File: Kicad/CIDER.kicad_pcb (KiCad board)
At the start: 4 copper layers, 74.9 x 57.1 mm, 69 parts, among them CN1 CDTV-DIAG, J1 JTAG, J2 LED, J3 A500_MODE, J4 Conn_02x22_Odd_Even, J5 To JP15, SW1 SW_DIP_x04, U1 AZ1117-3.3, U10 SST39SF010, U11 74LVC1G32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

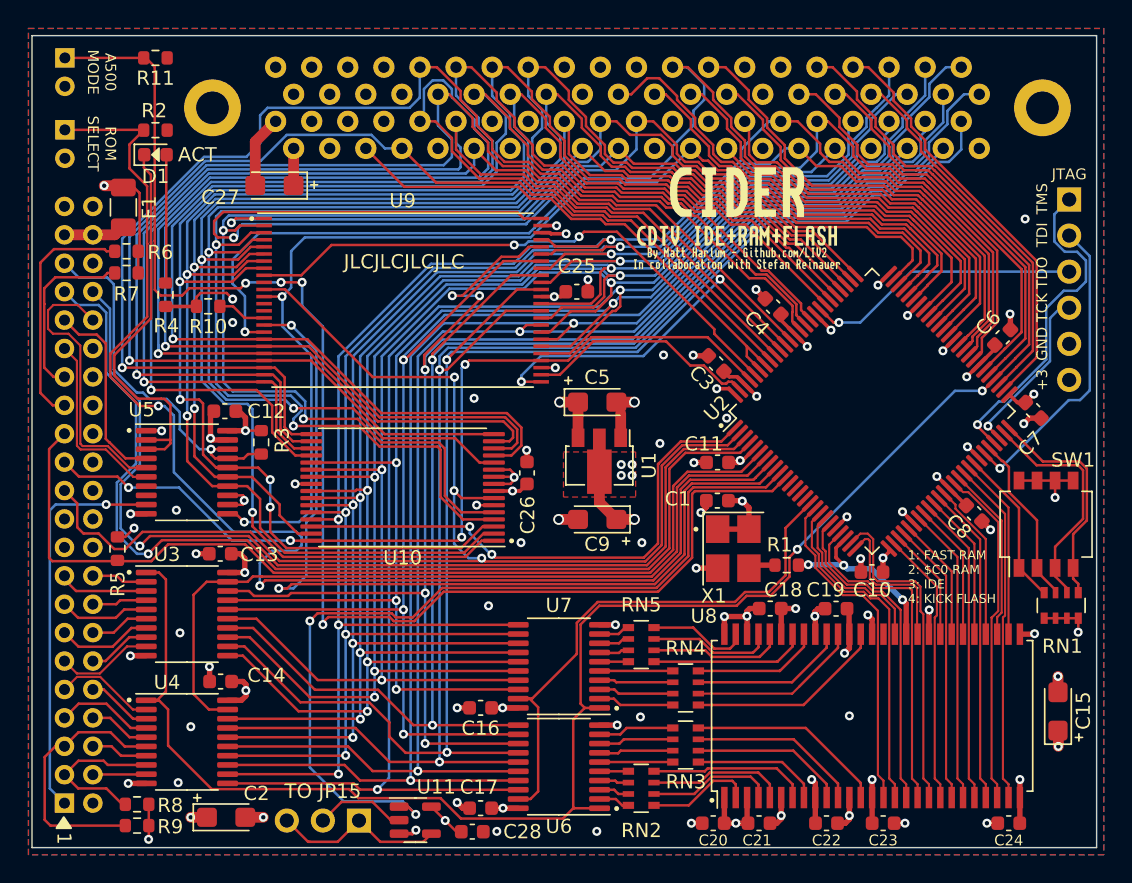
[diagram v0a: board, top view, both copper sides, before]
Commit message: Rev_A1: Add pull-down resistor for U11 input, add tooling holes
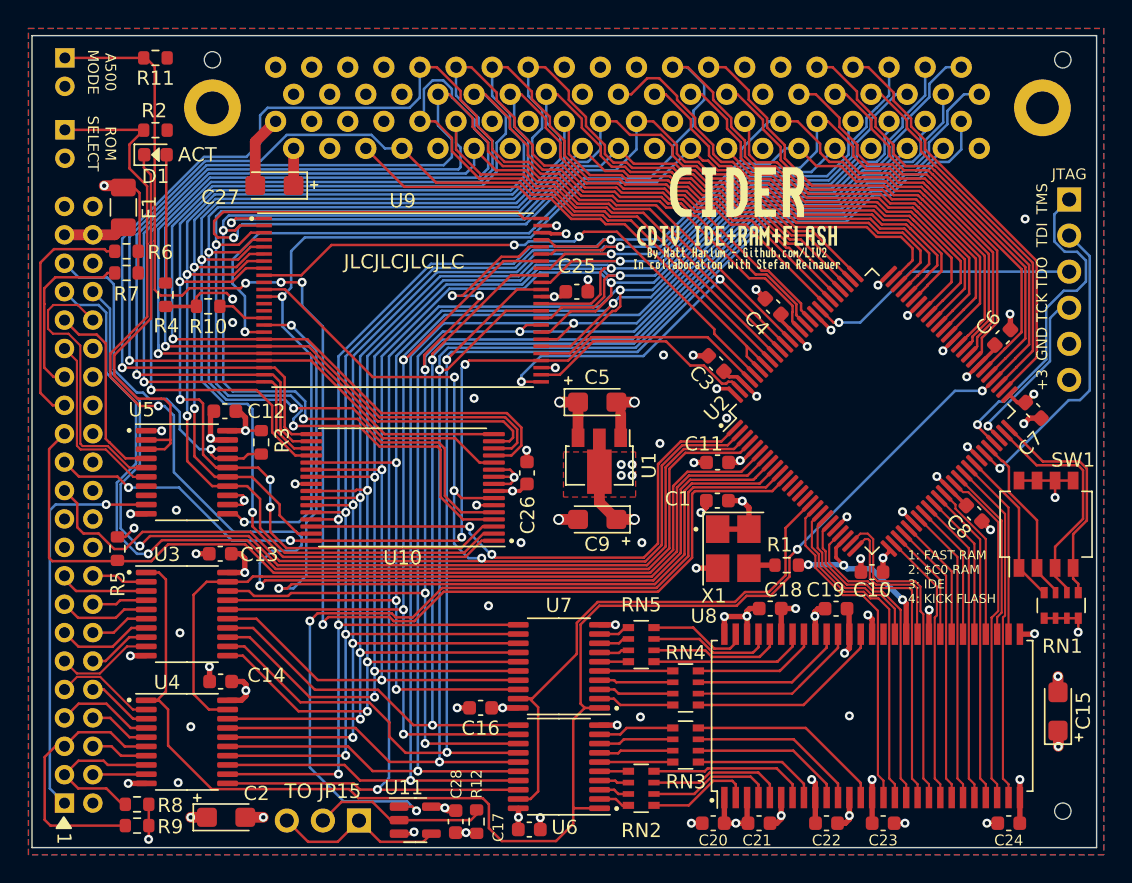
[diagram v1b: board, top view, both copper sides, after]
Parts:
- added ?: , , F.Cu at (178.0, 95.7)
- added R12: 10K, Resistor_SMD:R_0603_1608Metric, F.Cu at (136.7, 149.3)
- added REF**: jlc_assembly_toolinghole, JLC-Tooling:jlc_assembly_toolinghole, F.Cu at (178.0, 148.6)
- added REF**: jlc_assembly_toolinghole, JLC-Tooling:jlc_assembly_toolinghole, F.Cu at (118.1, 95.7)
- moved C17 3.74 mm to (140.4, 149.9), turned to 0 degrees
- moved C28 1.37 mm to (135.2, 149.3), turned to -90 degrees
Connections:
- net /Amiga+CPLD/NOEXT renamed /Amiga+CPLD/A500
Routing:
- net Net-(J5-Pad2): track 6.44 -> 12.4 mm
- net /Amiga+CPLD/R~{W}: track 130.7 -> 133.6 mm
- net VCC: track 43.8 -> 41.9 mm
- net GND: track 85.2 -> 86.2 mm, vias 70 -> 69
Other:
- board text added: "REV A1 APR 2023"
- board text removed: "REV A APR 2023"

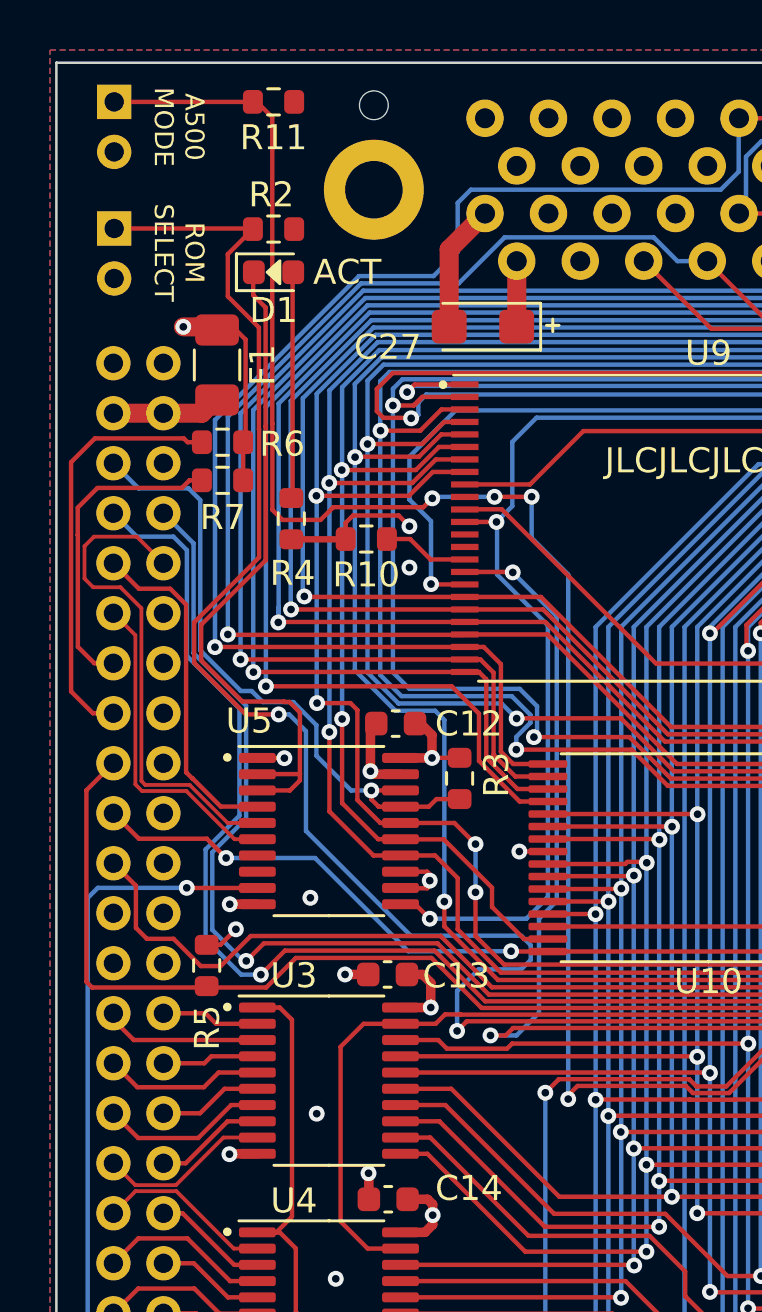
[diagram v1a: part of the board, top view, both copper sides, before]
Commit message: Rev-A1: Buffer A500/Bank Sel switches
Added inline resistors to these two and buffer them via U5
In Proto A it was found that operating the switches would cause latch-up and destroy the CPLD
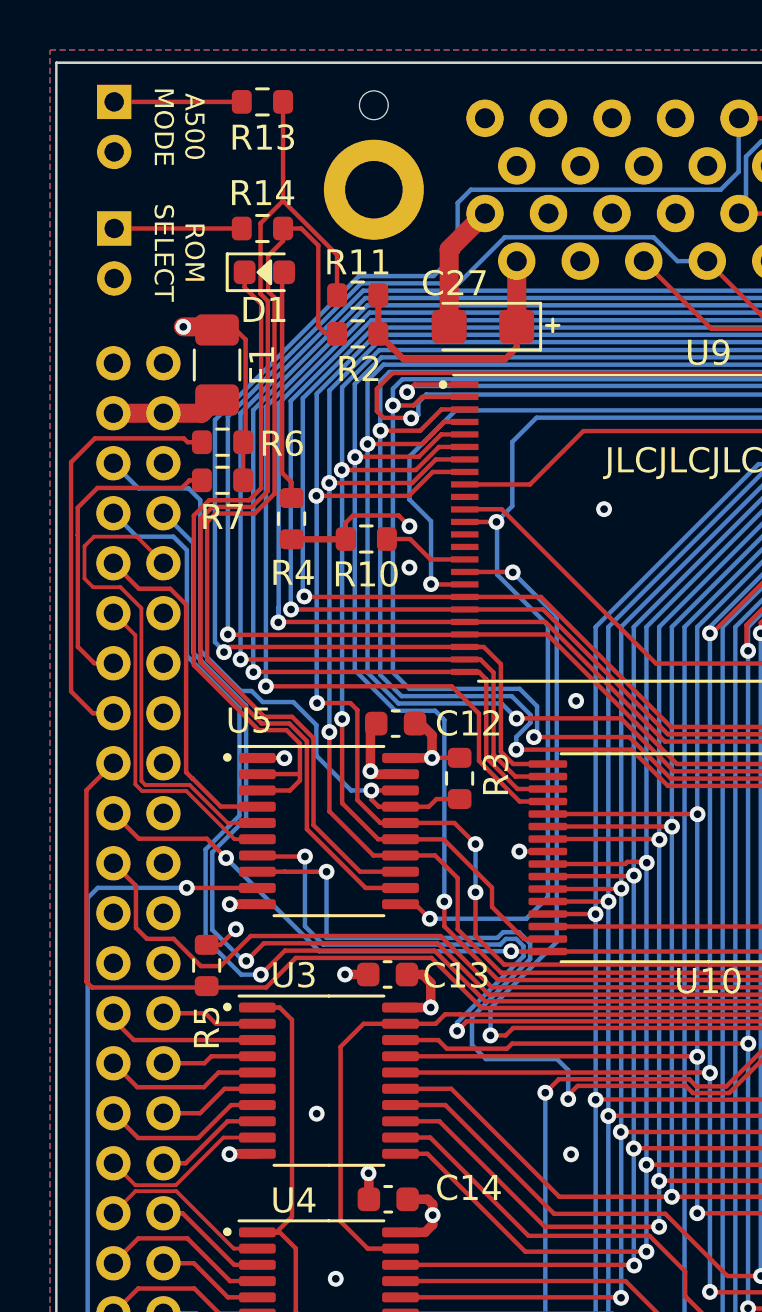
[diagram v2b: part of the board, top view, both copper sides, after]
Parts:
- added R13: 1K, Resistor_SMD:R_0603_1608Metric, F.Cu at (113.7, 95.5)
- added R14: 1K, Resistor_SMD:R_0603_1608Metric, F.Cu at (113.7, 100.6)
- U1: value AZ1117-3.3 -> AZ1117CR-3.3
- moved R11 8.43 mm to (117.5, 103.3)
- moved R2 5.38 mm to (117.5, 104.8)
- moved D1 0.37 mm to (113.7, 102.4)
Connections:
- J2 pad 1: /Amiga+CPLD/FLASH_BANK -> Net-(J2-Pad1)
- J2 pad 2: VCC -> GND
- J3 pad 1: /Amiga+CPLD/A500 -> Net-(J3-Pad1)
- J3 pad 2: VCC -> GND
- R11 pad 1: GND -> VCC
- R11 pad 2: /Amiga+CPLD/A500 -> /Amiga+CPLD/A500_SW
- R2 pad 1: GND -> VCC
- R2 pad 2: /Amiga+CPLD/FLASH_BANK -> /Amiga+CPLD/FLASH_BANK_SW
- U5 pad 12: GND -> /Amiga+CPLD/A500_SW
- U5 pad 13: GND -> /Amiga+CPLD/FLASH_BANK_SW
- U5 pad 7: unconnected-(U5-Pad7) -> /Amiga+CPLD/FLASH_BANK
- U5 pad 8: unconnected-(U5-Pad8) -> /Amiga+CPLD/A500
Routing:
- net /Amiga+CPLD/A500_SW: track 0.00 -> 43.4 mm
- net /Amiga+CPLD/FLASH_BANK_SW: track 0.00 -> 38.7 mm
- net /Amiga+CPLD/A500: track 97.5 -> 64.2 mm, vias 4 -> 2
- net /Amiga+CPLD/FLASH_BANK: track 93.1 -> 60.5 mm
- net VCC: track 41.9 -> 50.4 mm
- net Net-(J3-Pad1): track 0.00 -> 5.10 mm
- net Net-(J2-Pad1): track 0.00 -> 5.10 mm
- net GND: track 86.2 -> 83.3 mm, vias 69 -> 70
- net /IDE/~{LED}: track 27.9 -> 28.6 mm
- net /Amiga+CPLD/FLASH_A18: track 64.0 -> 63.3 mm

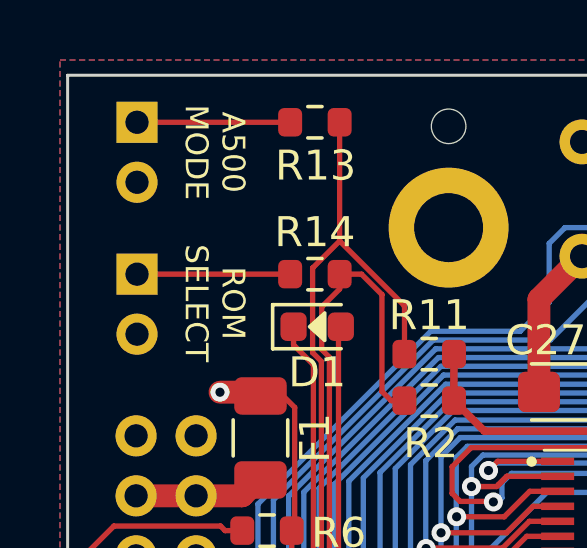
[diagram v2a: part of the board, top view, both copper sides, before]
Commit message: Rev-A1: move switch headers to top of the board and update render
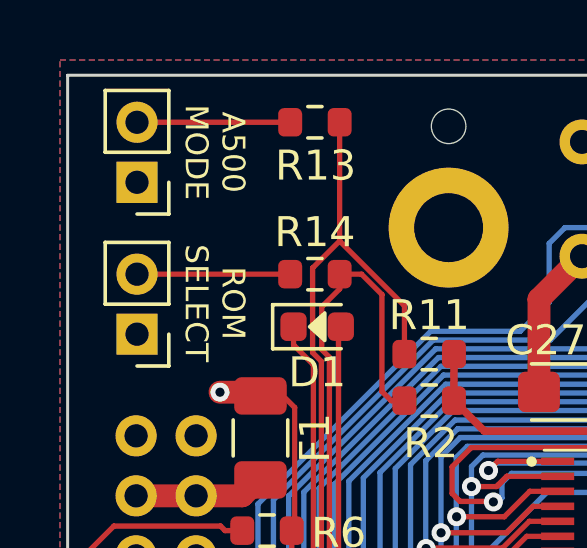
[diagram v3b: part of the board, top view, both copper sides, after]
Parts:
- J2, J3: moved to F.Cu
- moved J2 2.00 mm to (107.7, 102.6)
- moved J3 2.00 mm to (107.7, 97.5)
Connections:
- J2 pad 1: Net-(J2-Pad1) -> GND
- J2 pad 2: GND -> Net-(J2-Pad2)
- J3 pad 1: Net-(J3-Pad1) -> GND
- J3 pad 2: GND -> Net-(J3-Pad2)
- R13 pad 2: Net-(J3-Pad1) -> Net-(J3-Pad2)
- R14 pad 2: Net-(J2-Pad1) -> Net-(J2-Pad2)
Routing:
- net Net-(J3-Pad2): track 0.00 -> 5.10 mm
- net Net-(J3-Pad1): track 5.10 -> 0.00 mm
- net Net-(J2-Pad2): track 0.00 -> 5.10 mm
- net Net-(J2-Pad1): track 5.10 -> 0.00 mm
